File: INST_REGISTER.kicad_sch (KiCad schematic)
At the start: 22 parts, among them U16 74LS173, U17 74LS173, U18 74LS245

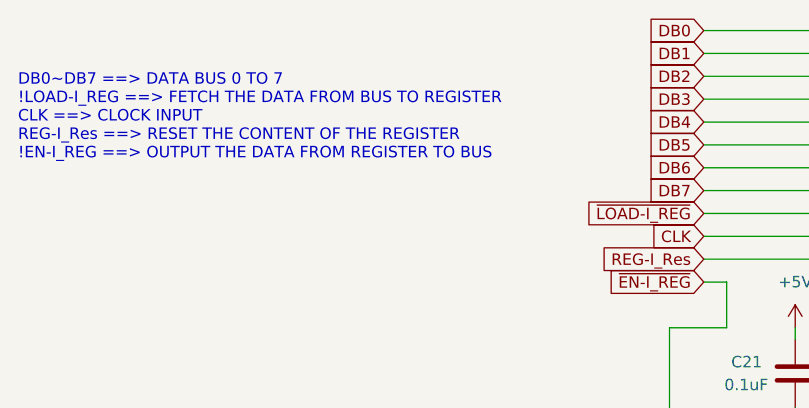
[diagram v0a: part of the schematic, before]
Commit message: Some inverting signal commands are modified
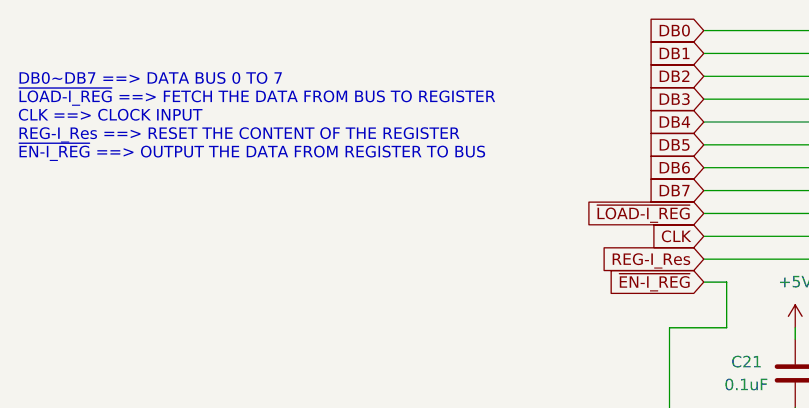
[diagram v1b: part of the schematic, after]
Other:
- note added: "DB0~DB7 ==> DATA BUS 0 TO 7 ~{LOAD-I_REG} ==> FETCH THE DATA FROM BUS TO REGISTER CLK ==> CLOCK INPUT REG-I_Res ==> RESET THE CONTENT OF THE REGISTER ~{EN-I_REG} ==> OUTPUT THE DATA FROM REGISTER TO BUS"
- note removed: "DB0~DB7 ==> DATA BUS 0 TO 7 !LOAD-I_REG ==> FETCH THE DATA FROM BUS TO REGISTER CLK ==> CLOCK INPUT REG-I_Res ==> RESET THE CONTENT OF THE REGISTER !EN-I_REG ==> OUTPUT THE DATA FROM REGISTER TO BUS"
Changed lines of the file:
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@@
 		)
 	)
-	(text "DB0~DB7 ==> DATA BUS 0 TO 7\n!LOAD-I_REG ==> FETCH THE DATA FROM BUS TO REGISTER\nCLK ==> CLOCK INPUT\nREG-I_Res ==> RESET THE CONTENT OF THE REGISTER\n!EN-I_REG ==> OUTPUT THE DATA FROM REGISTER TO BUS"
+	(text "DB0~DB7 ==> DATA BUS 0 TO 7\n~{LOAD-I_REG} ==> FETCH THE DATA FROM BUS TO REGISTER\nCLK ==> CLOCK INPUT\nREG-I_Res ==> RESET THE CONTENT OF THE REGISTER\n~{EN-I_REG} ==> OUTPUT THE DATA FROM REGISTER TO BUS"
 		(exclude_from_sim no)
 		(at 45.72 51.562 0)
